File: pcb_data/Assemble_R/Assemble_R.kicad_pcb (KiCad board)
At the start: 2 copper layers, 238.1 x 131 mm, 93 parts, among them U1 XIAO-nRF52840

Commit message: complete to design pattern of board R
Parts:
- moved DI9 21.2 mm to (228.0, 81.6)
- moved U1 1.79 mm to (238.7, 59.5)
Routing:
- net IO 7: track 0.00 -> 331.7 mm, vias 0 -> 1
- net IO 8: track 0.00 -> 286.9 mm
- net IO 10: track 0.00 -> 264.8 mm, vias 0 -> 3
- net Net-(D0-12-K): track 0.00 -> 243.7 mm
- net IO 9: track 0.00 -> 243.1 mm, vias 0 -> 4
- net Net-(D0-10-K): track 0.00 -> 237.6 mm
- net IO 12: track 0.00 -> 232.8 mm
- net IO 11: track 0.00 -> 232.4 mm
- net Net-(D0-9-K): track 0.00 -> 229.3 mm
- net Net-(D0-8-K): track 0.00 -> 229.1 mm
- net Net-(D1-7-K): track 0.00 -> 206.2 mm
- net Net-(D0-13-K): track 0.00 -> 193.7 mm
- net Net-(D0-11-K): track 0.00 -> 162.9 mm
- net IO 13: track 0.00 -> 160.0 mm, vias 0 -> 2
- net INTR_R: track 0.00 -> 113.6 mm
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- added copper zone on B.Cu, net GND
- added copper zone on F.Cu, net GND
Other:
- board size 238.1 x 131 mm -> 186.9 x 96.4 mm

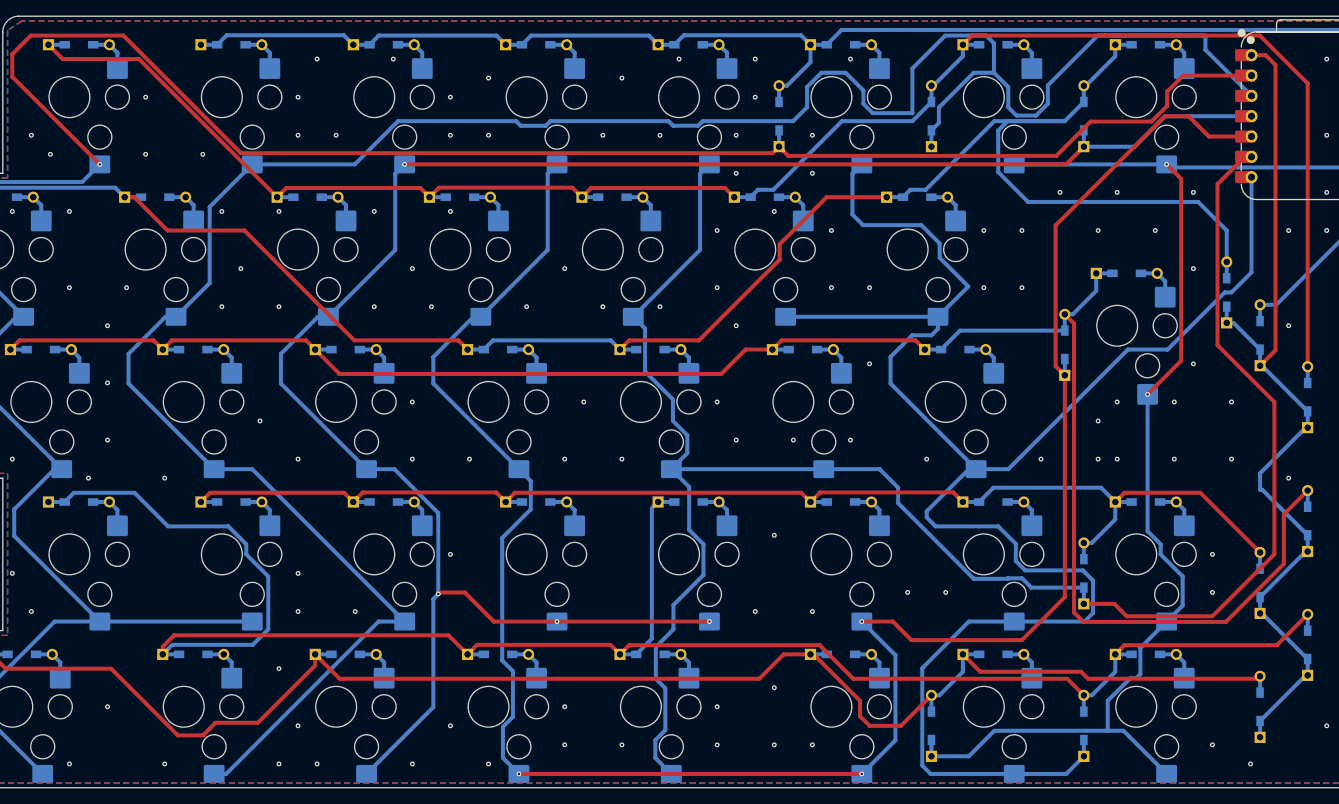
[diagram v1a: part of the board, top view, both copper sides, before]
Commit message: update foot print reference, and fix GND filling area DRC error
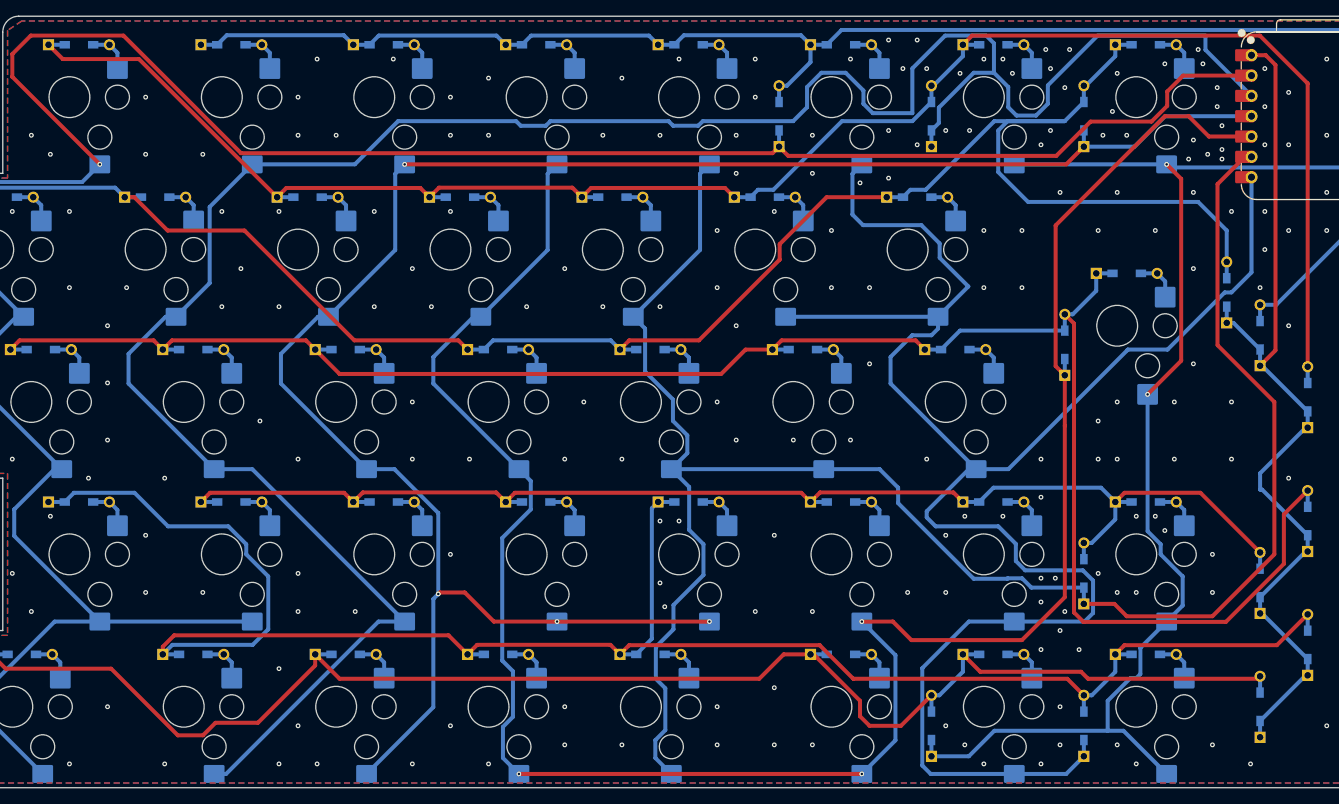
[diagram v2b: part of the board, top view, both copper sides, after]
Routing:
- net GND: vias 157 -> 234

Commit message: add mount hole (#5)
ネジ穴を追加しました．
特にレビュー項目はない（git logを綺麗に残すためのPR）のでセルフマージします．
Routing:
- net IO 7: track 331.7 -> 315.0 mm, vias 1 -> 2
- net Net-(D0-8-K): track 229.1 -> 230.0 mm
- net GND: vias 234 -> 240
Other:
- outline, holes or cut-outs redrawn

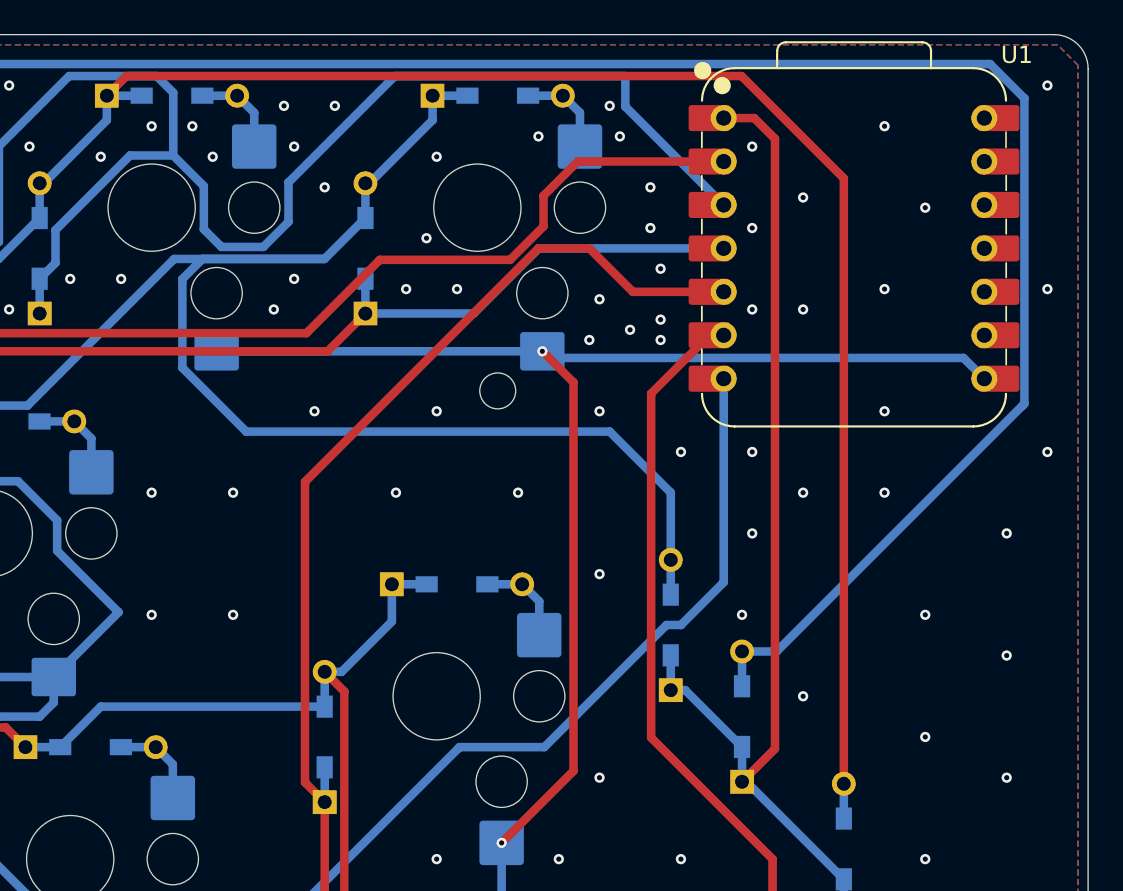
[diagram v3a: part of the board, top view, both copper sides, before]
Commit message: apply footprint update, and fix patterns
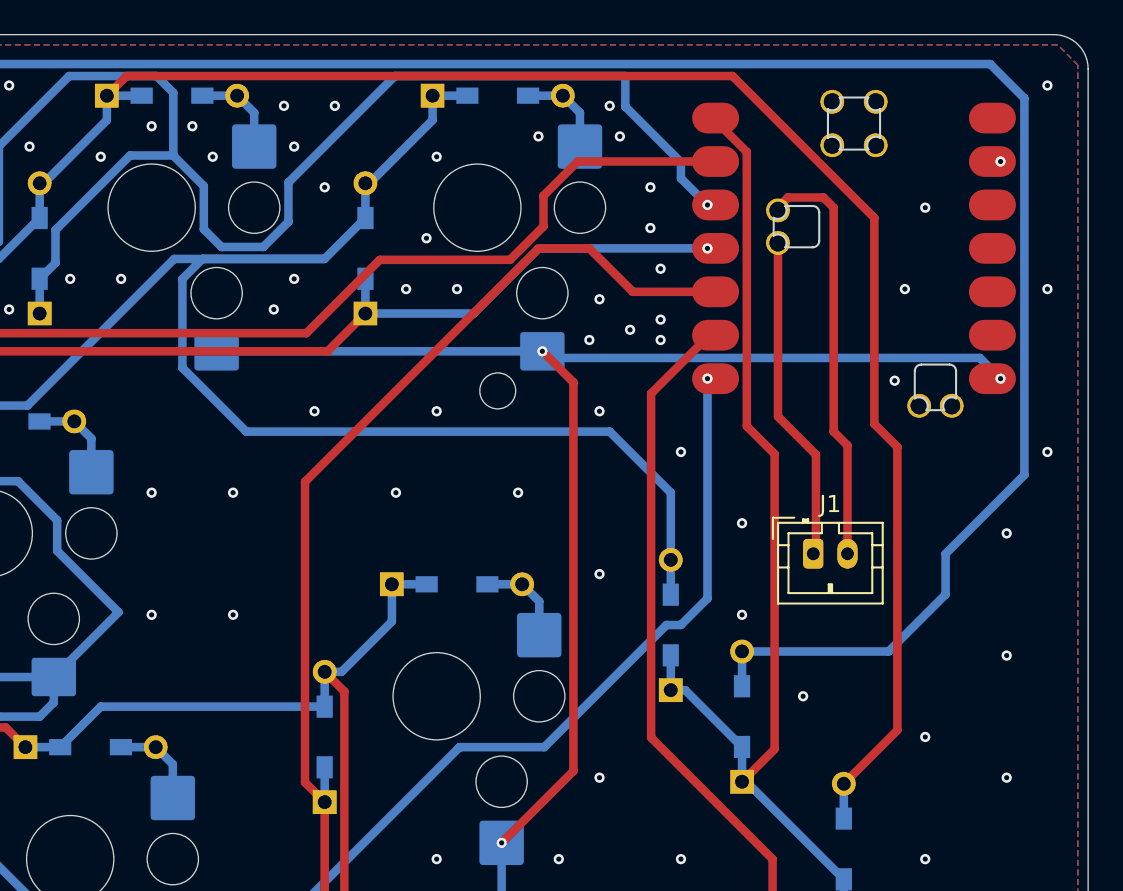
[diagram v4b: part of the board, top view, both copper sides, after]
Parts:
- added J1: Conn_01x02, Connector_JST:JST_PH_B2B-PH-K_1x02_P2.00mm_Vertical, F.Cu at (236.3, 77.4)
- U1: footprint Seeed Studio XIAO Series Library:XIAO-nRF52840-DIP -> mcu:xiao-ble-smd-cutout
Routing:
- net GND: track 0.00 -> 24.5 mm, vias 240 -> 231
- net BAT+: track 0.00 -> 19.2 mm
- net Net-(D1-7-K): track 206.2 -> 210.0 mm
- net Net-(D0-8-K): track 230.0 -> 232.3 mm
- net IO 9: track 243.1 -> 242.2 mm, vias 4 -> 5
- net IO 13: track 160.0 -> 160.9 mm, vias 2 -> 3
- net IO 8: track 286.9 -> 286.5 mm, vias 0 -> 1
- net IO 12: track 232.8 -> 232.4 mm, vias 0 -> 1

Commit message: add mount hole, and fix patterns
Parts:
- added H1: MountingHole, kbd_Hole:m2_Spacer_Hole, F.Cu at (83.3, 66.7)
- added H2: MountingHole, kbd_Hole:m2_Spacer_Hole, F.Cu at (159.5, 66.7)
- added H3: MountingHole, kbd_Hole:m2_Spacer_Hole, F.Cu at (207.2, 66.7)
- added H4: MountingHole, kbd_Hole:m2_Spacer_Hole, F.Cu at (92.9, 123.8)
- added H5: MountingHole, kbd_Hole:m2_Spacer_Hole, F.Cu at (169.1, 123.8)
- added H6: MountingHole, kbd_Hole:m2_Spacer_Hole, F.Cu at (226.2, 123.8)
- added H7: MountingHole, kbd_Hole:m2_Spacer_Hole, F.Cu at (235.7, 80.4)
- added H8: MountingHole, kbd_Hole:m2_Spacer_Hole, F.Cu at (131.0, 104.8)
- moved J1 7.71 mm to (243.7, 79.8)
- moved DI7 4.52 mm to (232.2, 91.4)
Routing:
- net Net-(D0-8-K): track 232.3 -> 243.0 mm
- net INTR_R: track 113.1 -> 106.3 mm
- net GND: track 24.5 -> 29.9 mm, vias 231 -> 228
- net BAT+: track 19.2 -> 24.5 mm
- net Net-(D1-7-K): track 210.0 -> 214.6 mm
- net IO 7: track 315.0 -> 318.1 mm
- net Net-(D0-12-K): track 243.7 -> 245.6 mm
- net IO 9: track 242.2 -> 243.9 mm
- net IO 13: track 160.9 -> 162.5 mm
- net Net-(D0-11-K): track 162.9 -> 163.9 mm
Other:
- outline, holes or cut-outs redrawn

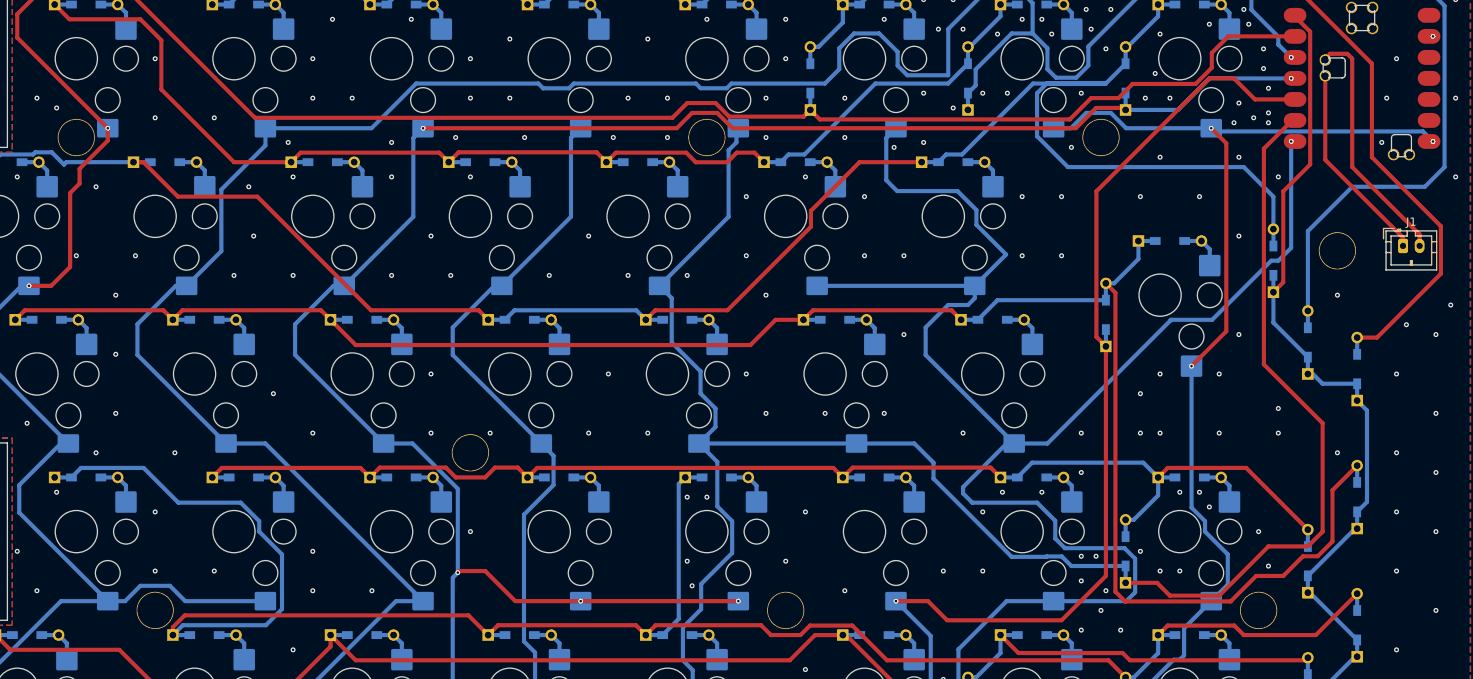
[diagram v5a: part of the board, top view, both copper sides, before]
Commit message: Issue/21 add capacitor bat gnd (#23)
* add Capacitor symbol

* add Capacitor foot print

* project file updated

* add model number of capacitor
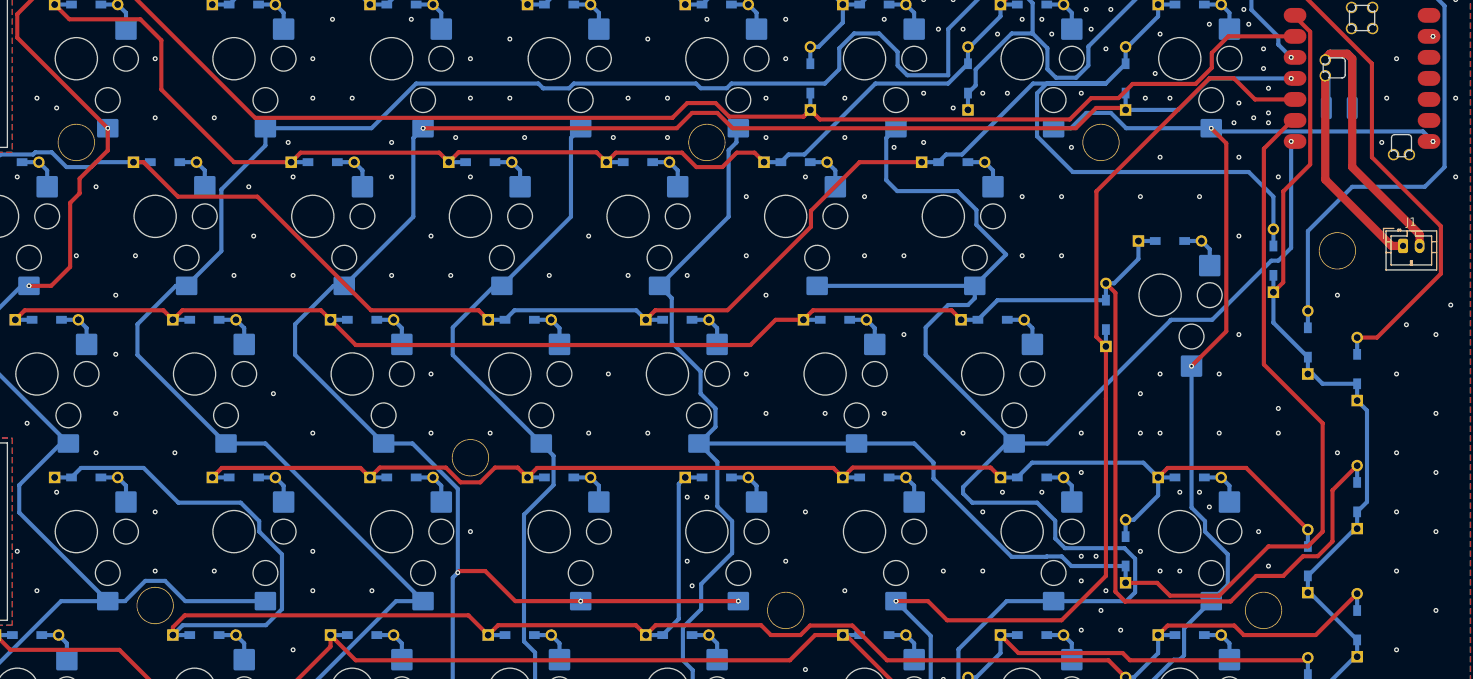
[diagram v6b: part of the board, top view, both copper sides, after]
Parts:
- added C1: C, Capacitor_SMD:C_1210_3225Metric_Pad1.33x2.70mm_HandSolder, B.Cu at (236.0, 63.1)
- moved H1 0.60 mm to (83.3, 67.3)
- moved H2 0.60 mm to (159.5, 67.3)
- moved H3 0.60 mm to (207.2, 67.3)
- moved H6 0.60 mm to (226.8, 123.8)
- moved H8 0.60 mm to (131.0, 105.4)
- moved H4 0.60 mm to (92.9, 123.2)
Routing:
- net GND: track 29.9 -> 39.8 mm
- net BAT+: track 24.5 -> 29.2 mm

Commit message: add model number of capacitor
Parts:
- C1: value C -> GRM32EC81C476KE15L
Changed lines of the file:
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@@
 			)
 		)
-		(property "Value" "C"
+		(property "Value" "GRM32EC81C476KE15L"
 			(at 0 -2.3 0)
 			(layer "B.Fab")
